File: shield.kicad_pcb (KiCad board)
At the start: 4 copper layers, 78.9 x 53.8 mm, 189 parts, among them J1 USB_C_Receptacle_USB2.0_14P, J10 BM03B-SRSS-TB, J2 USB_A, J3 USB_A, J4 BM03B-SRSS-TB, J5 BM03B-SRSS-TB, J6 BM03B-SRSS-TB, J7 Conn_ARM_JTAG_SWD_10, J9 BM03B-SRSS-TB, SW1 SW_Push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

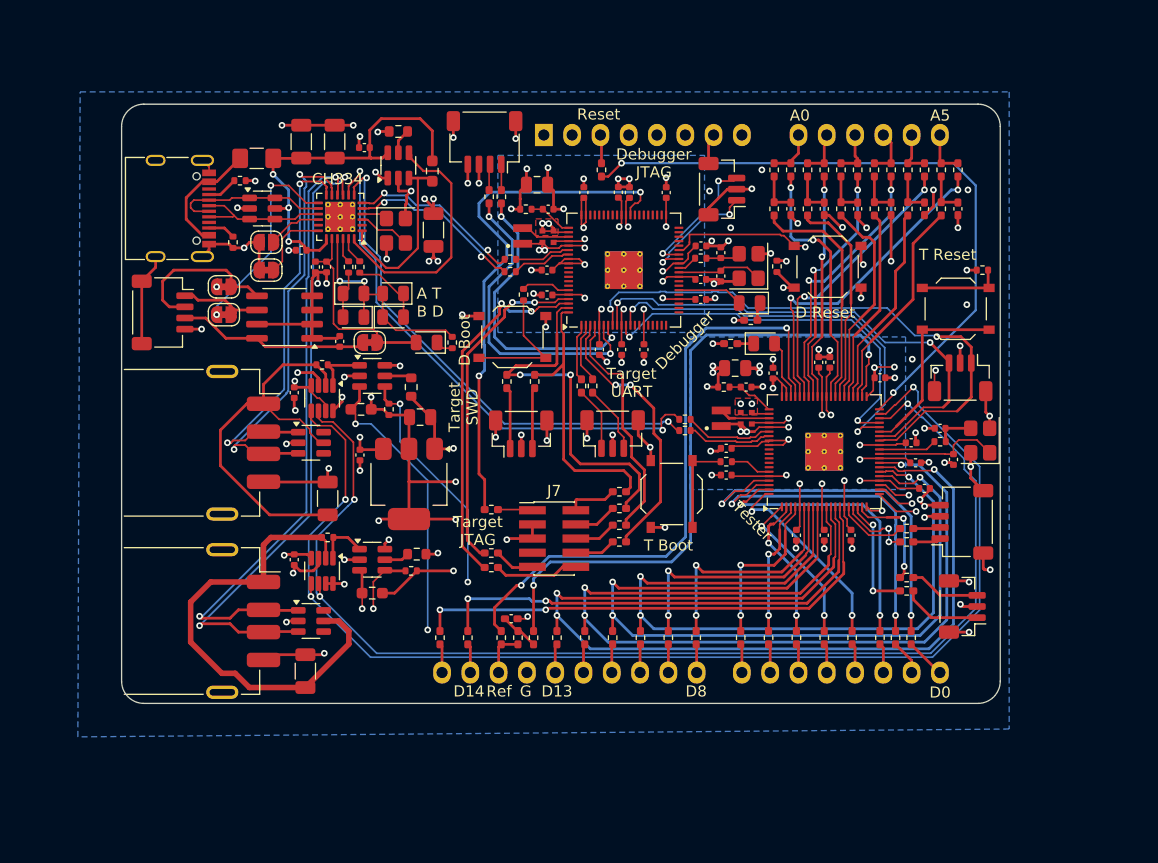
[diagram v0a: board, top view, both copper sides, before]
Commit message: Fix rev1 errors
Add USB mux to allow for USB PIO
Fix D+ D- mixup
Fix USB Hub LED indicator label
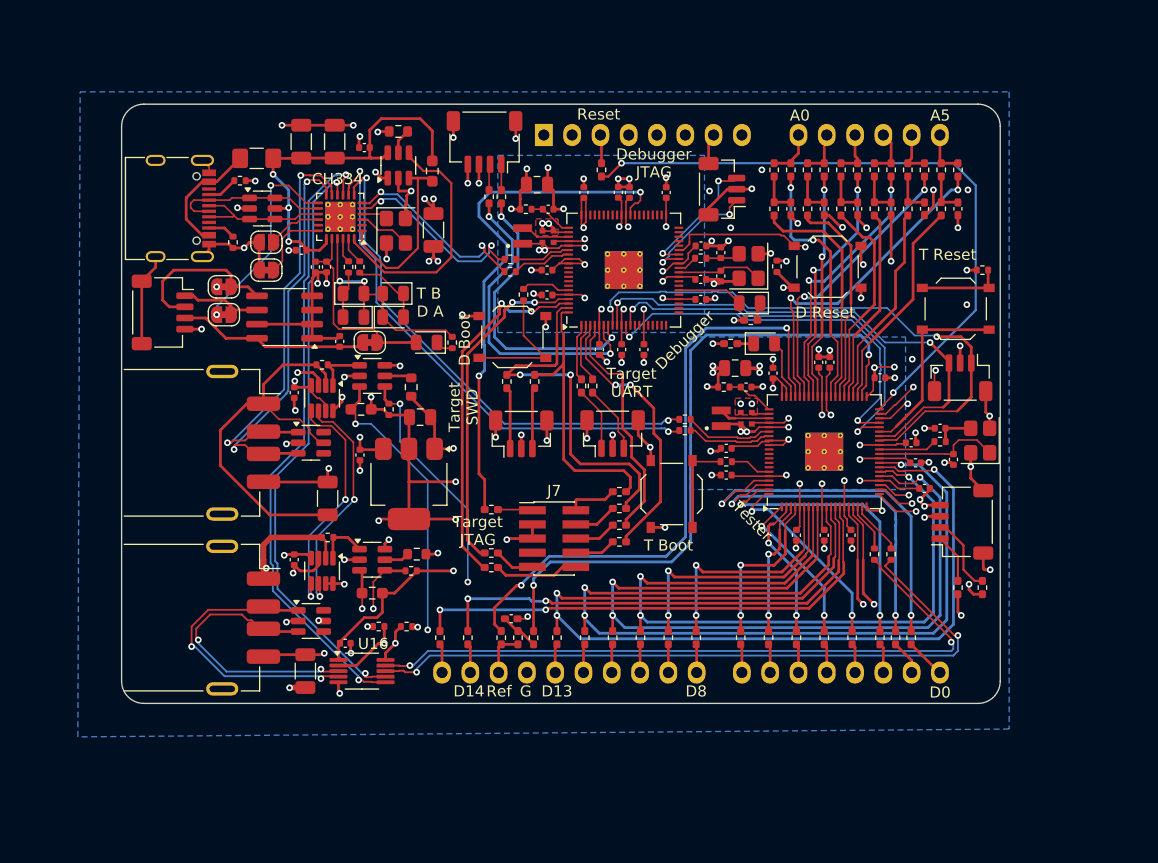
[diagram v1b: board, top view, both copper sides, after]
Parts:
- removed J10: BM03B-SRSS-TB, Connector_JST:JST_SH_BM03B-SRSS-TB_1x03-1MP_P1.00mm_Vertical
- removed R94, R95: 100R, Resistor_SMD:R_0402_1005Metric_Pad0.72x0.64mm_HandSolder
- added C50: 100nF, Capacitor_SMD:C_0402_1005Metric, F.Cu at (52.0, 79.5)
- added R53: 27, Resistor_SMD:R_0402_1005Metric, F.Cu at (99.5, 71.5)
- added R54: 27, Resistor_SMD:R_0402_1005Metric, F.Cu at (101.0, 71.5)
- added R55: 1K, Resistor_SMD:R_0402_1005Metric, F.Cu at (55.0, 78.0)
- added R56: 1K, Resistor_SMD:R_0402_1005Metric, F.Cu at (57.5, 78.0)
- added U16: FSUSB42MUX, Package_SO:MSOP-10_3x3mm_P0.5mm, F.Cu at (53.5, 82.0)
- moved R92 8.62 mm to (109.2, 74.5), turned to 90 degrees
- moved R93 6.16 mm to (107.0, 74.5), turned to 90 degrees
- moved J3 0.30 mm to (37.4, 77.2)
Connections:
- J3 pad 2: /USB/USB2.D- -> /USB Mux/USB.D-
- J3 pad 3: /USB/USB2.D+ -> /USB Mux/USB.D+
- R92 pad 1: /Tester/SDA -> /Tester/I2C.SDA
- R93 pad 1: /Tester/SCL -> /Tester/I2C.SCL
- U11 pad 1: /USB/USB2.D- -> /USB Mux/USB.D-
- U11 pad 3: /USB/USB2.D+ -> /USB Mux/USB.D+
- U13 pad 16: /Tester/SDA -> /Tester/~{USBH_EN}
- U13 pad 17: /Tester/SCL -> /Tester/USBH_SEL
- U13 pad 18: /Tester/TARGET_TX -> /Tester/HD+
- U13 pad 19: /Tester/TARGET_RX -> /Tester/HD-
- U4 pad 10: /USB/USB2.D- -> /USB Mux/USB1.D+
- U4 pad 11: /USB/USB1.D+ -> /USB/USB1.D-
- U4 pad 12: /USB/USB1.D- -> /USB/USB1.D+
- U4 pad 5: /USB/USB4.D+ -> /USB/USB4.D-
- U4 pad 6: /USB/USB4.D- -> /USB/USB4.D+
- U4 pad 7: /Tester/USB.D+ -> /Tester/USB.D-
- U4 pad 8: /Tester/USB.D- -> /Tester/USB.D+
- U4 pad 9: /USB/USB2.D+ -> /USB Mux/USB1.D-
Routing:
- net /Tester/USBH.D-: track 0.00 -> 63.7 mm, vias 0 -> 2
- net /Tester/USBH.D+: track 0.00 -> 62.6 mm, vias 0 -> 2
- net /Tester/USBH_SEL: track 0.00 -> 62.4 mm, vias 0 -> 2
- net /USB/USB2.D+: track 57.5 -> 0.00 mm, vias 2 -> 0
- net /Tester/~{USBH_EN}: track 0.00 -> 56.7 mm, vias 0 -> 2
- net /USB Mux/USB1.D-: track 0.00 -> 56.5 mm, vias 0 -> 2
- net /USB/USB2.D-: track 56.1 -> 0.00 mm, vias 2 -> 0
- net /USB Mux/USB1.D+: track 0.00 -> 53.5 mm, vias 0 -> 2
- net /USB Mux/USB.D-: track 0.00 -> 26.6 mm, vias 0 -> 2
- net /USB Mux/USB.D+: track 0.00 -> 25.4 mm, vias 0 -> 2
- net Net-(J3-VBUS): track 43.1 -> 27.1 mm, vias 0 -> 3
- net /Tester/TARGET_TX: track 10.8 -> 0.00 mm, vias 2 -> 0
- net /Tester/TARGET_RX: track 9.94 -> 0.00 mm, vias 2 -> 0
- net +3V3: track 152.4 -> 160.7 mm
- net Net-(J10-Pin_1): track 7.17 -> 0.00 mm
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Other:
- board text added: "T B D A"
- board text removed: "A T B D"

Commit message: Address board review comments
- Add pull-ups for both I2C busses (4K7)
- Set eFuse limit to 600mA (400mA before)
- Label StemmaQt as such in schematics
- Fix typo in USB Port value
- Fix USB Mux to be disabled by default (pull-down to pull-up)
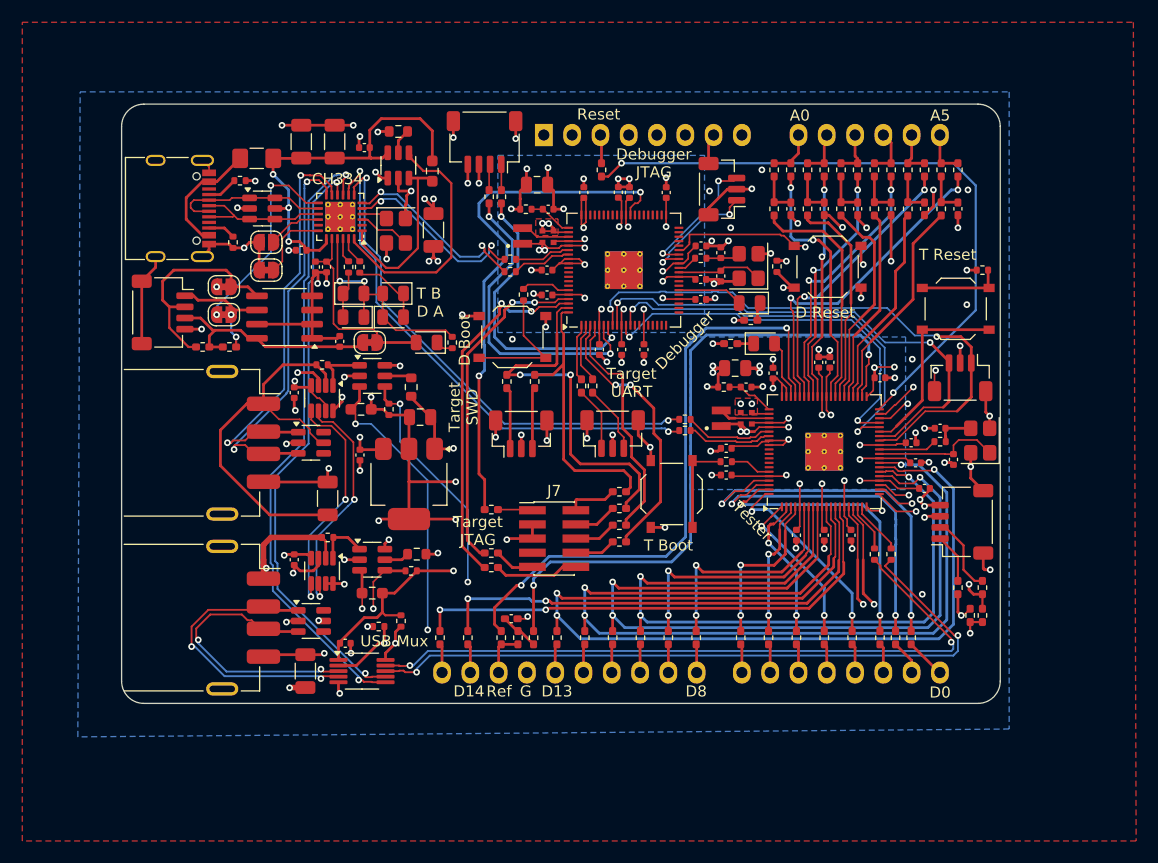
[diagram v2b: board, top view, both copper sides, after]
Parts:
- added R75: 4K7, Resistor_SMD:R_0402_1005Metric_Pad0.72x0.64mm_HandSolder, F.Cu at (109.2, 77.0)
- added R76: 4K7, Resistor_SMD:R_0402_1005Metric_Pad0.72x0.64mm_HandSolder, F.Cu at (108.1, 77.0)
- added R77: 4K7, Resistor_SMD:R_0402_1005Metric_Pad0.72x0.64mm_HandSolder, F.Cu at (39.2, 52.9)
- added R78: 4K7, Resistor_SMD:R_0402_1005Metric_Pad0.72x0.64mm_HandSolder, F.Cu at (41.6, 52.9)
- J1: value USB_C_Receptacle_USB2.0_14P -> USB_C_Receptacle_USB2.0_16P
- R3: value 150K -> 100K
- U1, U14, U17: value ~ -> StemmaQt
- moved R56 0.71 mm to (57.0, 77.5), turned to -90 degrees
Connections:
- R56 pad 1: /Tester/~{USBH_EN} -> +3V3
- R56 pad 2: GND -> /Tester/~{USBH_EN}
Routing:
- net /USB/SDA: track 14.4 -> 19.4 mm
- net +3V3: track 160.7 -> 164.5 mm, vias 41 -> 42
- net /USB/SCL: track 7.79 -> 10.9 mm, vias 0 -> 2
- net Net-(JP5-A): track 17.2 -> 20.1 mm
- net /Tester/I2C.SDA: track 109.5 -> 110.8 mm
- net /Tester/I2C.SCL: track 113.7 -> 114.7 mm
- net GND: track 204.3 -> 203.8 mm, vias 101 -> 102
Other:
- board text added: "USB Mux"
